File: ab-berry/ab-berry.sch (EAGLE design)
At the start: 34 parts, among them U1 LM1117MPX-3.3/NOPB or AP2114H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

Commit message: wip
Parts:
- H1, H2, H3, H4: value MOUNT-HOLE3.6 -> MOUNT-HOLE3.2; device holes:MOUNT-HOLE3.6 -> holes:MOUNT-HOLE3.2
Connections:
- net CAN_H: now also JP1.3, JP2.3; no longer JP1.2, JP2.2
- net CAN_L: now also JP1.2, JP2.2; no longer JP1.3, JP2.3
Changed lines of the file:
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@@
 <grid distance="0.1" unitdist="inch" unit="inch" style="lines" multiple="1" display="no" altdistance="0.01" altunitdist="inch" altunit="inch"/>
 <layers>
-<layer number="1" name="Top" color="4" fill="1" visible="no" active="no"/>
-<layer number="16" name="Bottom" color="1" fill="1" visible="no" active="no"/>
-<layer number="17" name="Pads" color="2" fill="1" visible="no" active="no"/>
-<layer number="18" name="Vias" color="2" fill="1" visible="no" active="no"/>
-<layer number="19" name="Unrouted" color="6" fill="1" visible="no" active="no"/>
-<layer number="20" name="Dimension" color="15" fill="1" visible="no" active="no"/>
-<layer number="21" name="tPlace" color="7" fill="1" visible="no" active="no"/>
-<layer number="22" name="bPlace" color="7" fill="1" visible="no" active="no"/>
-<layer number="23" name="tOrigins" color="15" fill="1" visible="no" active="no"/>
-<layer number="24" name="bOrigins" color="15" fill="1" visible="no" active="no"/>
-<layer number="25" name="tNames" color="7" fill="1" visible="no" active="no"/>
-<layer number="26" name="bNames" color="7" fill="1" visible="no" active="no"/>
-<layer number="27" name="tValues" color="7" fill="1" visible="no" active="no"/>
-<layer number="28" name="bValues" color="7" fill="1" visible="no" active="no"/>
+<layer number="1" name="Top" color="4" fill="1" visible="yes" active="no"/>
+<layer number="16" name="Bottom" color="1" fill="1" visible="yes" active="no"/>
+<layer number="17" name="Pads" color="2" fill="1" visible="yes" active="no"/>
+<layer number="18" name="Vias" color="2" fill="1" visible="yes" active="no"/>
+<layer number="19" name="Unrouted" color="6" fill="1" visible="yes" active="no"/>
+<layer number="20" name="Dimension" color="15" fill="1" visible="yes" active="no"/>
+<layer number="21" name="tPlace" color="7" fill="1" visible="yes" active="no"/>
+<layer number="22" name="bPlace" color="7" fill="1" visible="yes" active="no"/>
+<layer number="23" name="tOrigins" color="15" fill="1" visible="yes" active="no"/>
+<layer number="24" name="bOrigins" color="15" fill="1" visible="yes" active="no"/>
+<layer number="25" name="tNames" color="7" fill="1" visible="yes" active="no"/>
+<layer number="26" name="bNames" color="7" fill="1" visible="yes" active="no"/>
+<layer number="27" name="tValues" color="7" fill="1" visible="yes" active="no"/>
+<layer number="28" name="bValues" color="7" fill="1" visible="yes" active="no"/>
 <layer number="29" name="tStop" color="7" fill="3" visible="no" active="no"/>
 <layer number="30" name="bStop" color="7" fill="6" visible="no" active="no"/>
@@
 <layer number="35" name="tGlue" color="7" fill="4" visible="no" active="no"/>
 <layer number="36" name="bGlue" color="7" fill="5" visible="no" active="no"/>
-<layer number="37" name="tTest" color="7" fill="1" visible="no" active="no"/>
-<layer number="38" name="bTest" color="7" fill="1" visible="no" active="no"/>
+<layer number="37" name="tTest" color="7" fill="1" visible="yes" active="no"/>
+<layer number="38" name="bTest" color="7" fill="1" visible="yes" active="no"/>
 <layer number="39" name="tKeepout" color="4" fill="11" visible="no" active="no"/>
 <layer number="40" name="bKeepout" color="1" fill="11" visible="no" active="no"/>
@@
 <layer number="44" name="Drills" color="7" fill="1" visible="no" active="no"/>
 <layer number="45" name="Holes" color="7" fill="1" visible="no" active="no"/>
-<layer number="46" name="Milling" color="3" fill="1" visible="no" active="no"/>
-<layer number="47" name="Measures" color="7" fill="1" visible="no" active="no"/>
-<layer number="48" name="Document" color="7" fill="1" visible="no" active="no"/>
-<layer number="49" name="Reference" color="7" fill="1" visible="no" active="no"/>
-<layer number="50" name="dxf" color="7" fill="1" visible="no" active="no"/>
-<layer number="51" name="tDocu" color="7" fill="1" visible="no" active="no"/>
-<layer number="52" name="bDocu" color="7" fill="1" visible="no" active="no"/>
-<layer number="53" name="tGND_GNDA" color="7" fill="9" visible="no" active="no"/>
-<layer number="54" name="bGND_GNDA" color="1" fill="9" visible="no" active="no"/>
-<layer number="56" name="wert" color="7" fill="1" visible="no" active="no"/>
+<layer number="46" name="Milling" color="3" fill="1" visible="yes" active="no"/>
+<layer number="47" name="Measures" color="7" fill="1" visible="yes" active="no"/>
+<layer number="48" name="Document" color="7" fill="1" visible="yes" active="no"/>
+<layer number="49" name="Reference" color="7" fill="1" visible="yes" active="no"/>
+<layer number="50" name="dxf" color="7" fill="1" visible="yes" active="no"/>
+<layer number="51" name="tDocu" color="7" fill="1" visible="yes" active="no"/>
+<layer number="52" name="bDocu" color="7" fill="1" visible="yes" active="no"/>
+<layer number="53" name="tGND_GNDA" color="7" fill="9" visible="yes" active="no"/>
+<layer number="54" name="bGND_GNDA" color="1" fill="9" visible="yes" active="no"/>
+<layer number="56" name="wert" color="7" fill="1" visible="yes" active="no"/>
 <layer number="90" name="Modules" color="5" fill="1" visible="yes" active="yes"/>
 <layer number="91" name="Nets" color="2" fill="1" visible="yes" active="yes"/>
@@
 <part name="JP2" library="keves" deviceset="PINHD-1X4" device=""/>
 <part name="U$30" library="microbuilder" deviceset="GND" device=""/>
-<part name="H1" library="holes" deviceset="MOUNT-HOLE" device="3.6"/>
-<part name="H2" library="holes" deviceset="MOUNT-HOLE" device="3.6"/>
-<part name="H3" library="holes" deviceset="MOUNT-HOLE" device="3.6"/>
-<part name="H4" library="holes" deviceset="MOUNT-HOLE" device="3.6"/>
+<part name="H1" library="holes" deviceset="MOUNT-HOLE" device="3.2" value="MOUNT-HOLE3.2"/>
+<part name="H2" library="holes" deviceset="MOUNT-HOLE" device="3.2" value="MOUNT-HOLE3.2"/>
+<part name="H3" library="holes" deviceset="MOUNT-HOLE" device="3.2" value="MOUNT-HOLE3.2"/>
+<part name="H4" library="holes" deviceset="MOUNT-HOLE" device="3.2" value="MOUNT-HOLE3.2"/>
 <part name="U$29" library="microbuilder" deviceset="5.0V" device=""/>
 <part name="JP3" library="pinhead" deviceset="PINHD-1X2" device=""/>
@@
 </segment>
 <segment>
+<pinref part="JP1" gate="A" pin="3"/>
+<pinref part="JP2" gate="A" pin="3"/>
+<wire x1="-68.58" y1="38.1" x2="-53.34" y2="38.1" width="0.1524" layer="91"/>
+<wire x1="-68.58" y1="38.1" x2="-86.36" y2="38.1" width="0.1524" layer="91"/>
+<junction x="-68.58" y="38.1"/>
+<label x="-86.36" y="38.1" size="1.778" layer="95"/>
+</segment>
+</net>
+<net name="CAN_L" class="0">
+<segment>
+<pinref part="D1" gate="G$1" pin="CANL"/>
+<wire x1="50.8" y1="-27.94" x2="58.42" y2="-27.94" width="0.1524" layer="91"/>
+<label x="55.88" y="-27.94" size="1.778" layer="95"/>
+</segment>
+<segment>
 <pinref part="JP1" gate="A" pin="2"/>
 <pinref part="JP2" gate="A" pin="2"/>
@@
 </segment>
 </net>
-<net name="CAN_L" class="0">
-<segment>
-<pinref part="D1" gate="G$1" pin="CANL"/>
-<wire x1="50.8" y1="-27.94" x2="58.42" y2="-27.94" width="0.1524" layer="91"/>
-<label x="55.88" y="-27.94" size="1.778" layer="95"/>
-</segment>
-<segment>
-<pinref part="JP1" gate="A" pin="3"/>
-<pinref part="JP2" gate="A" pin="3"/>
-<wire x1="-68.58" y1="38.1" x2="-53.34" y2="38.1" width="0.1524" layer="91"/>
-<wire x1="-68.58" y1="38.1" x2="-86.36" y2="38.1" width="0.1524" layer="91"/>
-<junction x="-68.58" y="38.1"/>
-<label x="-86.36" y="38.1" size="1.778" layer="95"/>
-</segment>
-</net>

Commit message: ab-berry
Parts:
- added LED2: (no value), microbuilder:LED0603
- added R6: 330, microbuilder:RESISTOR0603
- C8, C9: value (none) -> 10uF Tantalum
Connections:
- new net N$6: R6.2, STM32F072CBT6.PB0/ADC_IN8/TIM3_CH3
- new net N$7: LED2.A, R6.1
- net GND: now also LED2.C
- net LCD_CS1: now also STM32F072CBT6.PB2
- net LCD_CS2: now also STM32F072CBT6.PB1/ADC_IN9/TIM3_CH4
- net LCD_DC: now also STM32F072CBT6.PA4/ADC_IN4/DAC_OUT1
- net LCD_RST: now also STM32F072CBT6.PA3/ADC_IN3/COMP2_INP/USART2_RX
- net ROT1_A: now also STM32F072CBT6.PB15/WKUP7/RTC_REFIN/SPI2_MOSI
- net ROT1_B: now also STM32F072CBT6.PB14/SPI2_MISO/I2C2_SDA
- net ROT1_SW: now also STM32F072CBT6.PB12
- net ROT2_A: now also STM32F072CBT6.PB4/SPI1_MISO/TIM3_CH1
- net ROT2_B: now also STM32F072CBT6.PB5/WKUP6/SPI1_MOSI/TIM3_CH2
- net ROT2_SW: now also STM32F072CBT6.PB3/SPI1_SCK/TIM2_CH2
- net ROT3_A: now also STM32F072CBT6.PB7/USART1_RX/I2C1_SDA
- net ROT3_B: now also STM32F072CBT6.PB8/I2C1_SCL/TIM16_CH1/CAN_RX
- net ROT3_SW: now also STM32F072CBT6.PB6USART1_TX/I2C1_SCL
- net ROT4_A: now also STM32F072CBT6.PB13/SPI2_SCK/I2C2_SCL
- net ROT4_B: now also STM32F072CBT6.PB11/I2C2_SDA/TIM2_C4/USART3_RX
- net ROT4_SW: now also STM32F072CBT6.PB10/I2C2_SCL/TIM2_CH3/USART3_TX

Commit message: ab-berry: added xtal :/
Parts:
- added C12, C13: 18pF, microbuilder:CAP_CERAMIC0603
- added U$36: ABM7-8.000MHZ-D2Y-T, keves:ABM7-8.000MHZ-D2Y-T
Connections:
- new net N$8: C12.P$2, STM32F072CBT6.PF0/OSC_IN, U$36.2
- new net N$9: C13.P$1, STM32F072CBT6.PF1/OSC_OUT, U$36.1
- net DBG_RX: now also TC1.8; no longer TC1.6
- net DBG_TX: now also TC1.6; no longer TC1.8
- net GND: now also C12.P$1, C13.P$2
- net ROT1_A: now also STM32F072CBT6.PB14/SPI2_MISO/I2C2_SDA; no longer STM32F072CBT6.PB15/WKUP7/RTC_REFIN/SPI2_MOSI
- net ROT1_B: now also STM32F072CBT6.PB15/WKUP7/RTC_REFIN/SPI2_MOSI; no longer STM32F072CBT6.PB14/SPI2_MISO/I2C2_SDA
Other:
- moved on the sheet: R1
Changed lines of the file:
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@@
 <?xml version="1.0" encoding="utf-8"?>
 <!DOCTYPE eagle SYSTEM "eagle.dtd">
-<eagle version="7.5.0">
+<eagle version="7.2.0">
 <drawing>
 <settings>
@@
 <part name="LED2" library="microbuilder" deviceset="LED" device="0603"/>
 <part name="U$33" library="microbuilder" deviceset="GND" device=""/>
+<part name="C12" library="microbuilder" deviceset="CAP_CERAMIC" device="0603" value="18pF"/>
+<part name="C13" library="microbuilder" deviceset="CAP_CERAMIC" device="0603" value="18pF"/>
+<part name="U$34" library="microbuilder" deviceset="GND" device=""/>
+<part name="U$35" library="microbuilder" deviceset="GND" device=""/>
+<part name="U$36" library="keves" deviceset="ABM7-8.000MHZ-D2Y-T" device=""/>
 </parts>
 <sheets>
@@
 <instance part="U$7" gate="G$1" x="-20.32" y="38.1" rot="R270"/>
 <instance part="U$8" gate="G$1" x="-20.32" y="33.02" rot="R270"/>
-<instance part="R1" gate="G$1" x="7.62" y="25.4" rot="R90"/>
-<instance part="U$4" gate="G$1" x="7.62" y="15.24"/>
+<instance part="R1" gate="G$1" x="-5.08" y="25.4" rot="R90"/>
+<instance part="U$4" gate="G$1" x="-5.08" y="15.24"/>
 <instance part="D1" gate="G$1" x="38.1" y="-25.4"/>
 <instance part="R2" gate="G$1" x="17.78" y="-35.56" rot="R180"/>
@@
 <instance part="LED2" gate="G$1" x="149.86" y="40.64"/>
 <instance part="U$33" gate="G$1" x="160.02" y="40.64" rot="R90"/>
+<instance part="C12" gate="G$1" x="12.7" y="20.32" rot="R90"/>
+<instance part="C13" gate="G$1" x="10.16" y="15.24" rot="R270"/>
+<instance part="U$34" gate="G$1" x="5.08" y="15.24" rot="R270"/>
+<instance part="U$35" gate="G$1" x="5.08" y="20.32" rot="R270"/>
+<instance part="U$36" gate="G$1" x="17.78" y="17.78" rot="R90"/>
 </instances>
 <busses>
@@
 <pinref part="R1" gate="G$1" pin="1"/>
 <pinref part="U$4" gate="G$1" pin="GND"/>
-<wire x1="7.62" y1="17.78" x2="7.62" y2="20.32" width="0.1524" layer="91"/>
+<wire x1="-5.08" y1="17.78" x2="-5.08" y2="20.32" width="0.1524" layer="91"/>
 </segment>
 <segment>
@@
 <pinref part="U$33" gate="G$1" pin="GND"/>
 <wire x1="157.48" y1="40.64" x2="152.4" y2="40.64" width="0.1524" layer="91"/>
+</segment>
+<segment>
+<pinref part="C13" gate="G$1" pin="P$2"/>
+<pinref part="U$34" gate="G$1" pin="GND"/>
+</segment>
+<segment>
+<pinref part="C12" gate="G$1" pin="P$1"/>
+<pinref part="U$35" gate="G$1" pin="GND"/>
 </segment>
 </net>
@@
 <net name="DBG_TX" class="0">
 <segment>
+<pinref part="STM32F072CBT6" gate="G$1" pin="PA9/USART1_TX/TIM1_CH2"/>
+<wire x1="116.84" y1="63.5" x2="124.46" y2="63.5" width="0.1524" layer="91"/>
+<label x="121.92" y="63.5" size="1.778" layer="95"/>
+</segment>
+<segment>
+<pinref part="TC1" gate="A" pin="6"/>
+<wire x1="-2.54" y1="38.1" x2="5.08" y2="38.1" width="0.1524" layer="91"/>
+<label x="2.54" y="38.1" size="1.778" layer="95"/>
+</segment>
+</net>
+<net name="DBG_RX" class="0">
+<segment>
+<pinref part="STM32F072CBT6" gate="G$1" pin="PA10/USART1_RX/TIM1_CH3"/>
+<wire x1="116.84" y1="60.96" x2="124.46" y2="60.96" width="0.1524" layer="91"/>
+<label x="121.92" y="60.96" size="1.778" layer="95"/>
+</segment>
+<segment>
 <pinref part="TC1" gate="A" pin="8"/>
 <wire x1="-2.54" y1="35.56" x2="5.08" y2="35.56" width="0.1524" layer="91"/>
 <label x="2.54" y="35.56" size="1.778" layer="95"/>
 </segment>
-<segment>
-<pinref part="STM32F072CBT6" gate="G$1" pin="PA9/USART1_TX/TIM1_CH2"/>
-<wire x1="116.84" y1="63.5" x2="124.46" y2="63.5" width="0.1524" layer="91"/>
-<label x="121.92" y="63.5" size="1.778" layer="95"/>
-</segment>
-</net>
-<net name="DBG_RX" class="0">
-<segment>
-<pinref part="STM32F072CBT6" gate="G$1" pin="PA10/USART1_RX/TIM1_CH3"/>
-<wire x1="116.84" y1="60.96" x2="124.46" y2="60.96" width="0.1524" layer="91"/>
-<label x="121.92" y="60.96" size="1.778" layer="95"/>
-</segment>
-<segment>
-<pinref part="TC1" gate="A" pin="6"/>
-<wire x1="-2.54" y1="38.1" x2="5.08" y2="38.1" width="0.1524" layer="91"/>
-<label x="2.54" y="38.1" size="1.778" layer="95"/>
-</segment>
 </net>
 <net name="N$1" class="0">
@@
 <pinref part="STM32F072CBT6" gate="G$1" pin="BOOT0(P44)"/>
 <pinref part="R1" gate="G$1" pin="2"/>
-<wire x1="22.86" y1="30.48" x2="7.62" y2="30.48" width="0.1524" layer="91"/>
+<wire x1="22.86" y1="30.48" x2="-5.08" y2="30.48" width="0.1524" layer="91"/>
 </segment>
 </net>
@@
 </segment>
 <segment>
+<pinref part="STM32F072CBT6" gate="G$1" pin="PB14/SPI2_MISO/I2C2_SDA"/>
+<wire x1="116.84" y1="5.08" x2="124.46" y2="5.08" width="0.1524" layer="91"/>
+<label x="121.92" y="5.08" size="1.778" layer="95"/>
+</segment>
+</net>
+<net name="ROT1_B" class="0">
+<segment>
+<pinref part="ROT1" gate="G$1" pin="CH_B"/>
+<wire x1="-60.96" y1="5.08" x2="-76.2" y2="5.08" width="0.1524" layer="91"/>
+<label x="-81.28" y="5.08" size="1.778" layer="95"/>
+</segment>
+<segment>
 <pinref part="STM32F072CBT6" gate="G$1" pin="PB15/WKUP7/RTC_REFIN/SPI2_MOSI"/>
 <wire x1="116.84" y1="2.54" x2="124.46" y2="2.54" width="0.1524" layer="91"/>
@@
 </segment>
 </net>
-<net name="ROT1_B" class="0">
-<segment>
-<pinref part="ROT1" gate="G$1" pin="CH_B"/>
-<wire x1="-60.96" y1="5.08" x2="-76.2" y2="5.08" width="0.1524" layer="91"/>
-<label x="-81.28" y="5.08" size="1.778" layer="95"/>
-</segment>
-<segment>
-<pinref part="STM32F072CBT6" gate="G$1" pin="PB14/SPI2_MISO/I2C2_SDA"/>
-<wire x1="116.84" y1="5.08" x2="124.46" y2="5.08" width="0.1524" layer="91"/>
-<label x="121.92" y="5.08" size="1.778" layer="95"/>
-</segment>
-</net>
 <net name="ROT1_SW" class="0">
 <segment>
@@
 </segment>
 </net>
+<net name="N$8" class="0">
+<segment>
+<pinref part="C12" gate="G$1" pin="P$2"/>
+<pinref part="STM32F072CBT6" gate="G$1" pin="PF0/OSC_IN"/>
+<wire x1="15.24" y1="20.32" x2="17.78" y2="20.32" width="0.1524" layer="91"/>
+<pinref part="U$36" gate="G$1" pin="2"/>
+<wire x1="17.78" y1="20.32" x2="22.86" y2="20.32" width="0.1524" layer="91"/>
+<junction x="17.78" y="20.32"/>
+</segment>
+</net>
+<net name="N$9" class="0">
+<segment>
+<pinref part="C13" gate="G$1" pin="P$1"/>
+<pinref part="STM32F072CBT6" gate="G$1" pin="PF1/OSC_OUT"/>
+<wire x1="15.24" y1="15.24" x2="17.78" y2="15.24" width="0.1524" layer="91"/>
+<wire x1="17.78" y1="15.24" x2="22.86" y2="15.24" width="0.1524" layer="91"/>
+<wire x1="22.86" y1="15.24" x2="22.86" y2="17.78" width="0.1524" layer="91"/>
+<pinref part="U$36" gate="G$1" pin="1"/>
+<junction x="17.78" y="15.24"/>
+</segment>
+</net>

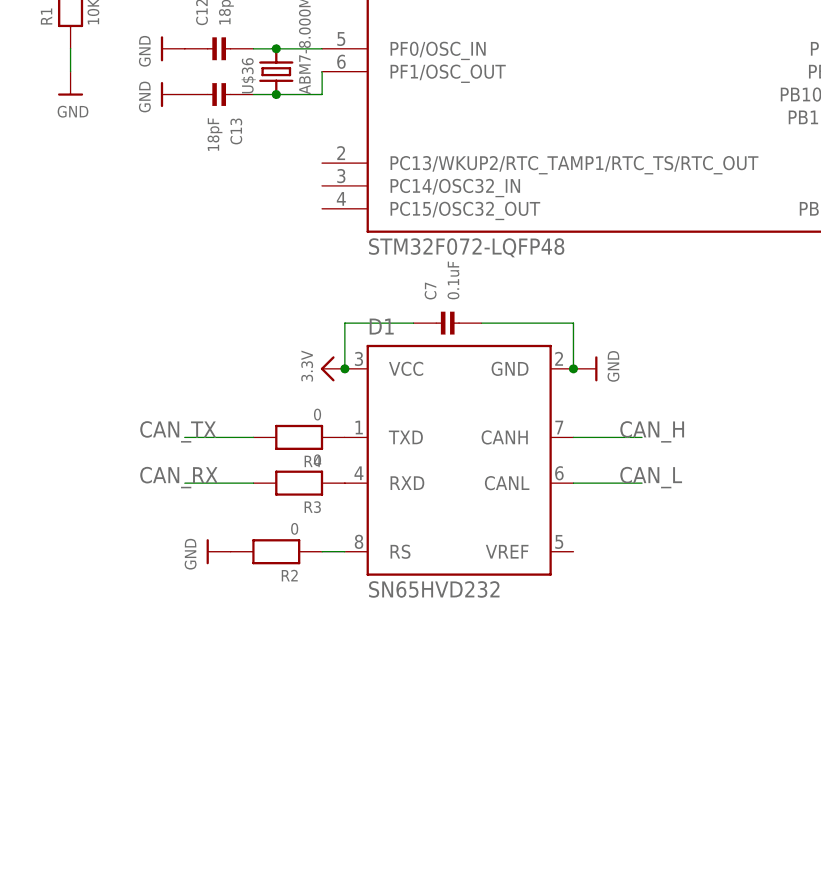
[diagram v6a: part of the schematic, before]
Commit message: add pushbutton
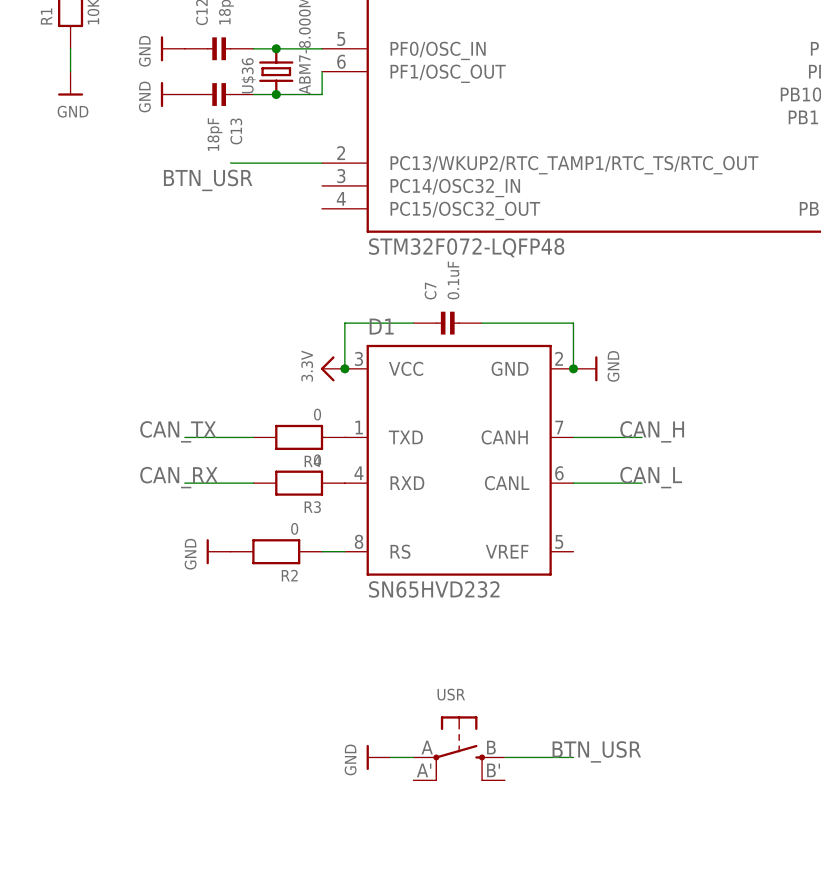
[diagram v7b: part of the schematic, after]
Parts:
- added USR: (no value), microbuilder:SWITCH_TACT_SMT
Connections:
- new net BTN_USR: STM32F072CBT6.PC13/WKUP2/RTC_TAMP1/RTC_TS/RTC_OUT, USR.S
- net GND: now also USR.P
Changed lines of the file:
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@@
 <part name="U$35" library="microbuilder" deviceset="GND" device=""/>
 <part name="U$36" library="keves" deviceset="ABM7-8.000MHZ-D2Y-T" device=""/>
+<part name="USR" library="microbuilder" deviceset="SWITCH_TACT_SMT" device=""/>
+<part name="U$37" library="microbuilder" deviceset="GND" device=""/>
 </parts>
 <sheets>
@@
 <instance part="U$35" gate="G$1" x="5.08" y="20.32" rot="R270"/>
 <instance part="U$36" gate="G$1" x="17.78" y="17.78" rot="R90"/>
+<instance part="USR" gate="G$1" x="38.1" y="-58.42"/>
+<instance part="U$37" gate="G$1" x="27.94" y="-58.42" rot="R270"/>
 </instances>
 <busses>
@@
 <pinref part="C12" gate="G$1" pin="P$1"/>
 <pinref part="U$35" gate="G$1" pin="GND"/>
+</segment>
+<segment>
+<pinref part="USR" gate="G$1" pin="P"/>
+<pinref part="U$37" gate="G$1" pin="GND"/>
+<wire x1="30.48" y1="-58.42" x2="33.02" y2="-58.42" width="0.1524" layer="91"/>
 </segment>
 </net>
@@
 </segment>
 </net>
+<net name="BTN_USR" class="0">
+<segment>
+<pinref part="USR" gate="G$1" pin="S"/>
+<wire x1="43.18" y1="-58.42" x2="50.8" y2="-58.42" width="0.1524" layer="91"/>
+<label x="48.26" y="-58.42" size="1.778" layer="95"/>
+</segment>
+<segment>
+<pinref part="STM32F072CBT6" gate="G$1" pin="PC13/WKUP2/RTC_TAMP1/RTC_TS/RTC_OUT"/>
+<wire x1="22.86" y1="7.62" x2="12.7" y2="7.62" width="0.1524" layer="91"/>
+<label x="5.08" y="5.08" size="1.778" layer="95"/>
+</segment>
+</net>
